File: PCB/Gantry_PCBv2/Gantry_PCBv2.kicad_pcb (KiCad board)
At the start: 2 copper layers, 120 x 120 mm, 64 parts, among them J1 Conn_01x14, J10 B2B-XH-A_LF__SN_, J11 B2B-XH-A_LF__SN_, J12 B2B-XH-A_LF__SN_, J13 Conn_01x03_Pin, J14 USB_C_Receptacle_USB2.0_16P, J17 B2B-XH-A_LF__SN_, J2 Conn_01x14, J3 Conn_01x10, J4 Screw_Terminal_01x02, J5 DCJ200-10-A-XX-X_REVA, J6 Conn_01x04_Pin, J7 Conn_01x04_Pin, J8 Conn_01x04_Pin, J9 Conn_01x04_Pin, Q1 SS8050, Q2 SS8050, SW7 SW_0, SW8 SW_EN, U1 ESP32-WROOM-32E, U2 CH340C, U3 TB6612FNG H-bridge Motor Driv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, U4 LM2576S-5, U5 AMS1117-3.3, U6 DRV8825_STEPPER_MOTOR_DRIVER_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, U7 DRV8825_STEPPER_MOTOR_DRIVER_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, U8 DRV8825_STEPPER_MOTOR_DRIVER_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, U9 DRV8825_STEPPER_MOTOR_DRIVER_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

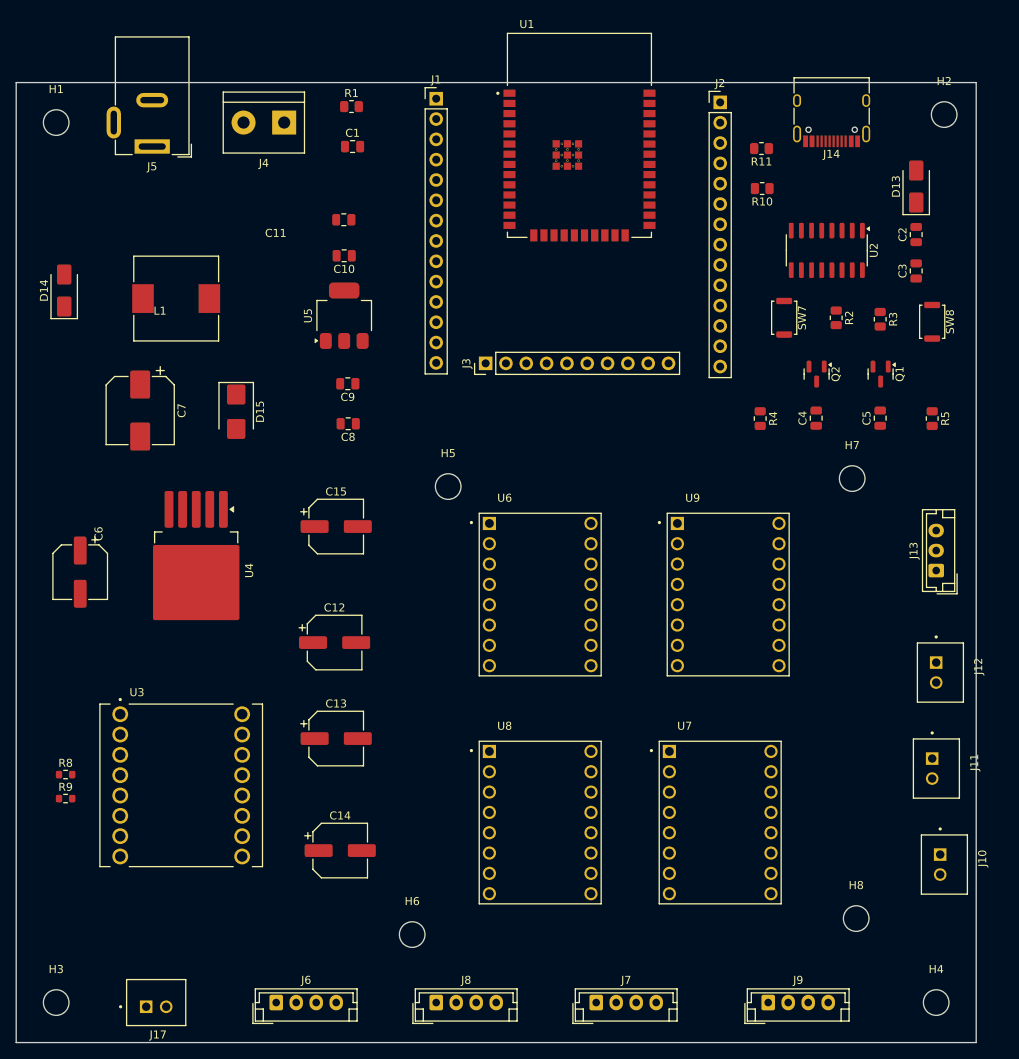
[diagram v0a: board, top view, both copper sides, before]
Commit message: complete PCB without silkscreen
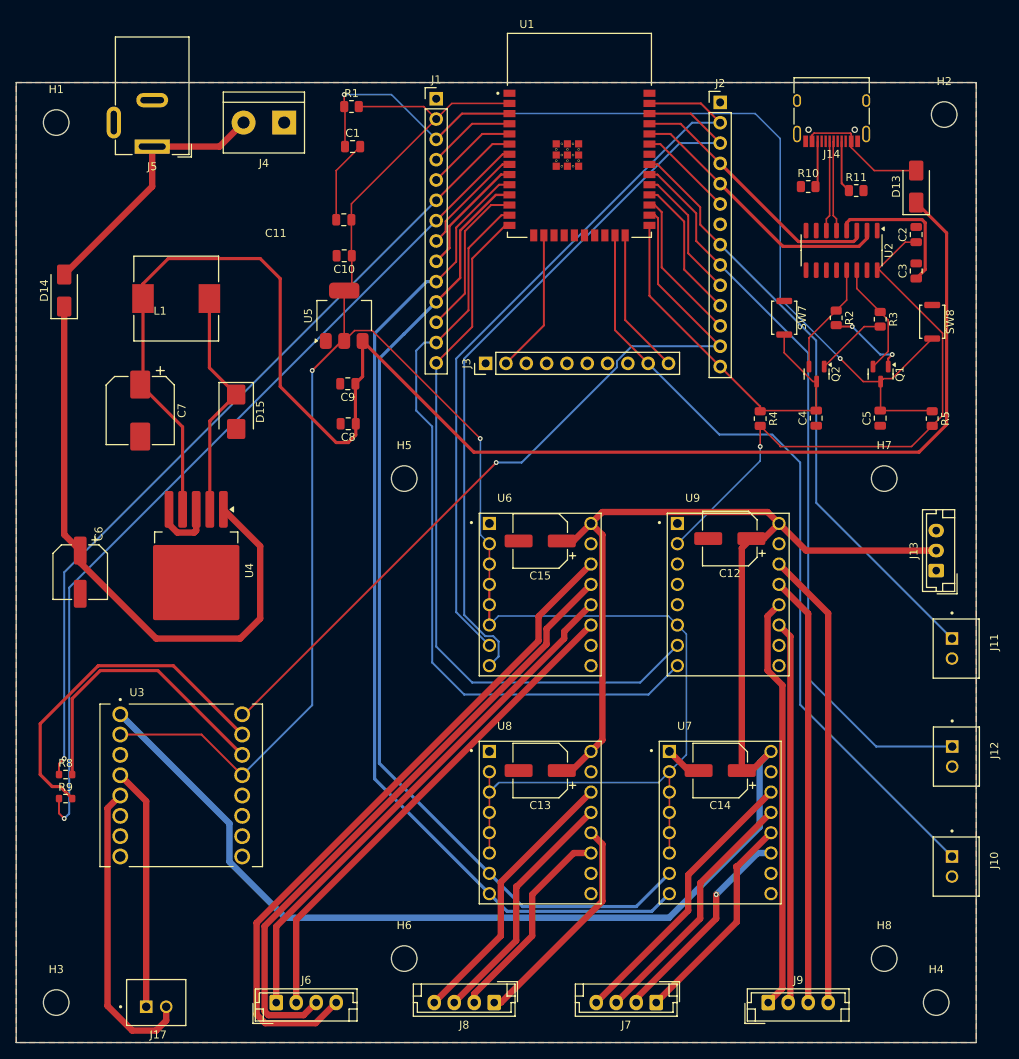
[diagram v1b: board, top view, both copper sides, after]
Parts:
- moved C12 51.1 mm to (139.2, 107.0), turned to 180 degrees
- moved C14 48.5 mm to (138.0, 136.0), turned to 180 degrees
- moved C13 25.8 mm to (115.5, 136.0), turned to 180 degrees
- moved C15 25.6 mm to (115.5, 107.3), turned to 180 degrees
- moved J11 15.2 mm to (167.5, 120.8)
- moved R11 12.9 mm to (155.0, 63.5), turned to 0 degrees
- moved J12 10.7 mm to (167.5, 134.2)
- moved J7 7.50 mm to (130.0, 165.0), turned to 180 degrees
- moved J8 7.25 mm to (109.8, 165.0), turned to 180 degrees
- moved H8 6.10 mm to (158.5, 159.5)
- moved R10 5.76 mm to (149.0, 63.0), turned to 0 degrees
- moved H5 5.59 mm to (98.5, 99.5)
- moved H7 4.00 mm to (158.5, 99.5)
- moved H6 3.16 mm to (98.5, 159.5)
- moved U2 1.85 mm to (153.2, 71.0)
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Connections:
- C8 pad 1: /5V_P -> /5V
- C9 pad 1: /5V_P -> /5V
- D13 pad 1: /5V_P -> /5V
- R8 pad 1: /18 -> /34
- R9 pad 1: /13 -> /35
- U3 pad 10: /35 -> unconnected-(U3-PWMB-Pad10)
- U5 pad 3: /5V_P -> /5V
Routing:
- net /3V3: track 0.06 -> 346.9 mm, vias 0 -> 3
- net /12V_P: track 0.00 -> 231.0 mm
- net /5V: track 0.00 -> 197.9 mm
- net /EN: track 0.00 -> 132.2 mm, vias 0 -> 2
- net /25: track 0.00 -> 127.3 mm
- net /26: track 0.59 -> 124.2 mm
- net /35: track 0.00 -> 109.4 mm, vias 0 -> 1
- net /34: track 0.00 -> 103.4 mm, vias 0 -> 1
- net /4: track 0.00 -> 99.7 mm, vias 0 -> 1
- net /15: track 0.00 -> 99.0 mm
- net /14: track 0.00 -> 96.8 mm
- net /22: track 0.00 -> 94.8 mm
- net /18: track 0.00 -> 93.3 mm
- net /23: track 0.00 -> 92.6 mm
- net /12: track 0.00 -> 90.7 mm
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- added copper zone on B.Cu, net GND
- added copper zone on F.Cu, net GND

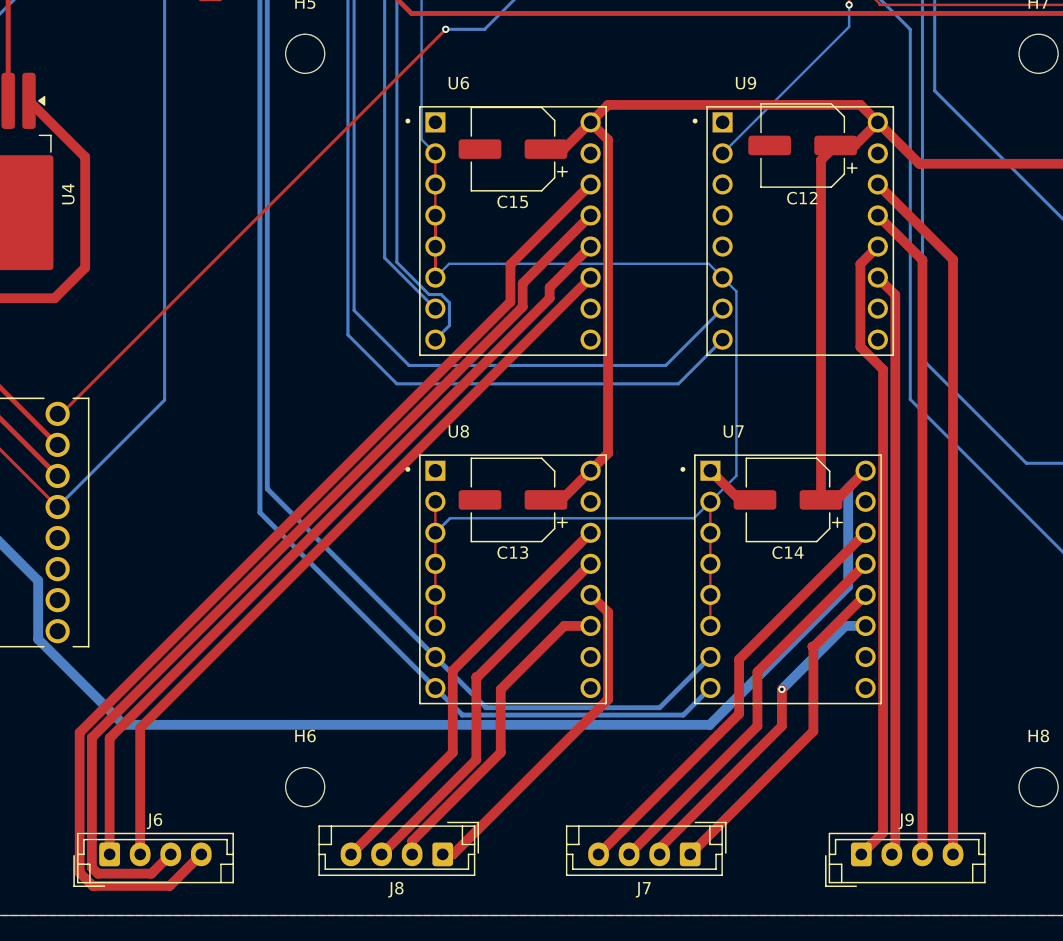
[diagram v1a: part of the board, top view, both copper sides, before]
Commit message: final PCB Rounting without silkscreen
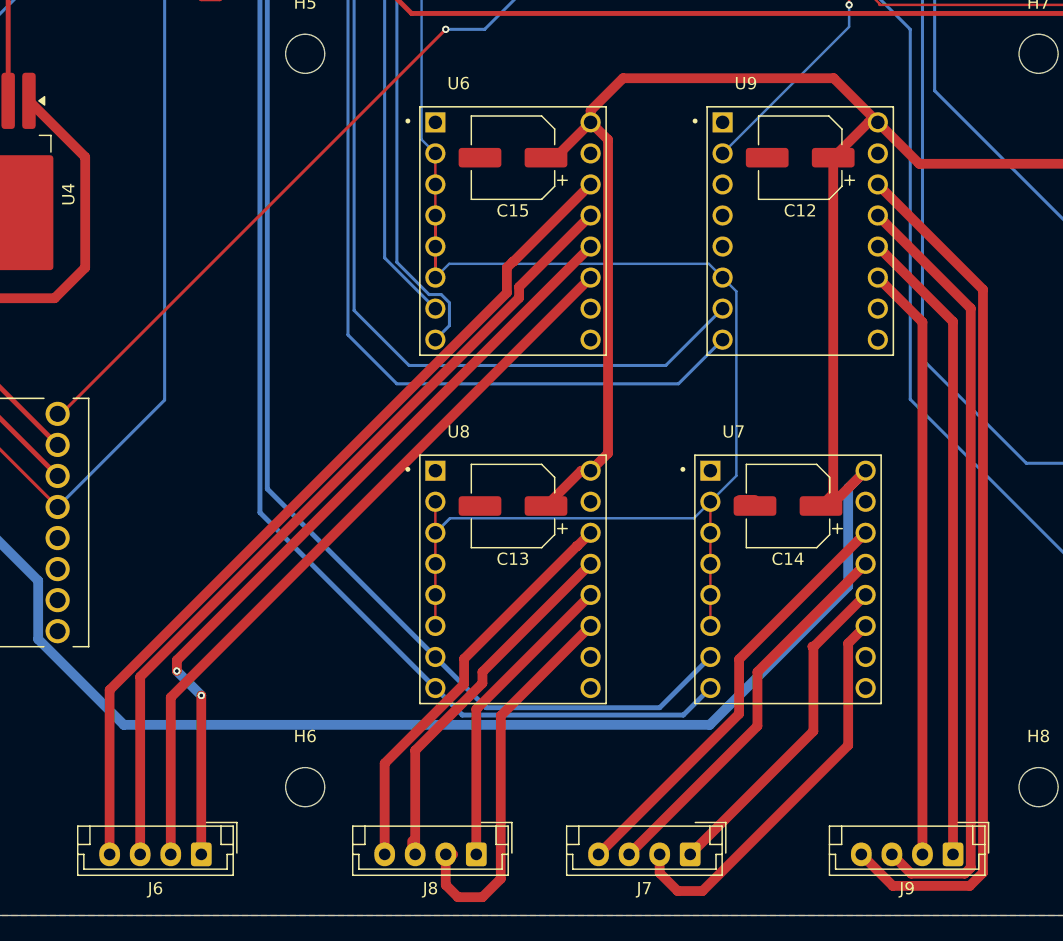
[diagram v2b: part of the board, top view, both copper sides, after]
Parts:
- moved J6 7.50 mm to (90.0, 165.0), turned to 180 degrees
- moved J9 7.50 mm to (151.5, 165.0), turned to 180 degrees
- moved J8 2.75 mm to (112.5, 165.0)
- moved C12 1.02 mm to (139.0, 108.0)
- moved C15 0.70 mm to (115.5, 108.0)
- moved C13 0.50 mm to (115.5, 136.5)
- moved C14 0.50 mm to (138.0, 136.5)
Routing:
- net /SM1_B2: track 57.4 -> 71.3 mm
- net /SM2_B2: track 85.1 -> 71.1 mm
- net /SM1_B1: track 53.8 -> 64.2 mm
- net /SM2_B1: track 77.6 -> 67.5 mm
- net /SM3_A2: track 26.6 -> 33.4 mm, vias 1 -> 0
- net /SM4_A2: track 26.0 -> 32.6 mm
- net GND: track 23.5 -> 20.1 mm
- net /12V_P: track 231.0 -> 234.1 mm
- net /SM4_A1: track 27.9 -> 25.1 mm
- net /SM2_A1: track 66.0 -> 64.6 mm, vias 0 -> 2
- net /SM4_B2: track 34.4 -> 33.3 mm
- net /SM2_A2: track 62.5 -> 61.4 mm
- net /SM1_A2: track 47.9 -> 48.7 mm

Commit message: Schematic v3
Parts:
- moved J6 7.50 mm to (82.5, 165.0), turned to 0 degrees
- moved J9 7.50 mm to (144.0, 165.0), turned to 0 degrees
- moved J8 2.75 mm to (109.8, 165.0)
- moved C12 1.02 mm to (139.2, 107.0)
- moved C15 0.70 mm to (115.5, 107.3)
- moved C13 0.50 mm to (115.5, 136.0)
- moved C14 0.50 mm to (138.0, 136.0)
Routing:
- net /SM1_B2: track 71.3 -> 57.4 mm
- net /SM2_B2: track 71.1 -> 85.1 mm
- net /SM1_B1: track 64.2 -> 53.8 mm
- net /SM2_B1: track 67.5 -> 77.6 mm
- net /SM3_A2: track 33.4 -> 26.6 mm, vias 0 -> 1
- net /SM4_A2: track 32.6 -> 26.0 mm
- net GND: track 20.1 -> 23.5 mm
- net /12V_P: track 234.1 -> 231.0 mm
- net /SM4_A1: track 25.1 -> 27.9 mm
- net /SM2_A1: track 64.6 -> 66.0 mm, vias 2 -> 0
- net /SM4_B2: track 33.3 -> 34.4 mm
- net /SM2_A2: track 61.4 -> 62.5 mm
- net /SM1_A2: track 48.7 -> 47.9 mm
